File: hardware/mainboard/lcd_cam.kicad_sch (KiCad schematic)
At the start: 59 parts, among them U17 PCA9306, U18 PCA9306, U19 ADP5070ACPZ, U20 CAT4106HV4

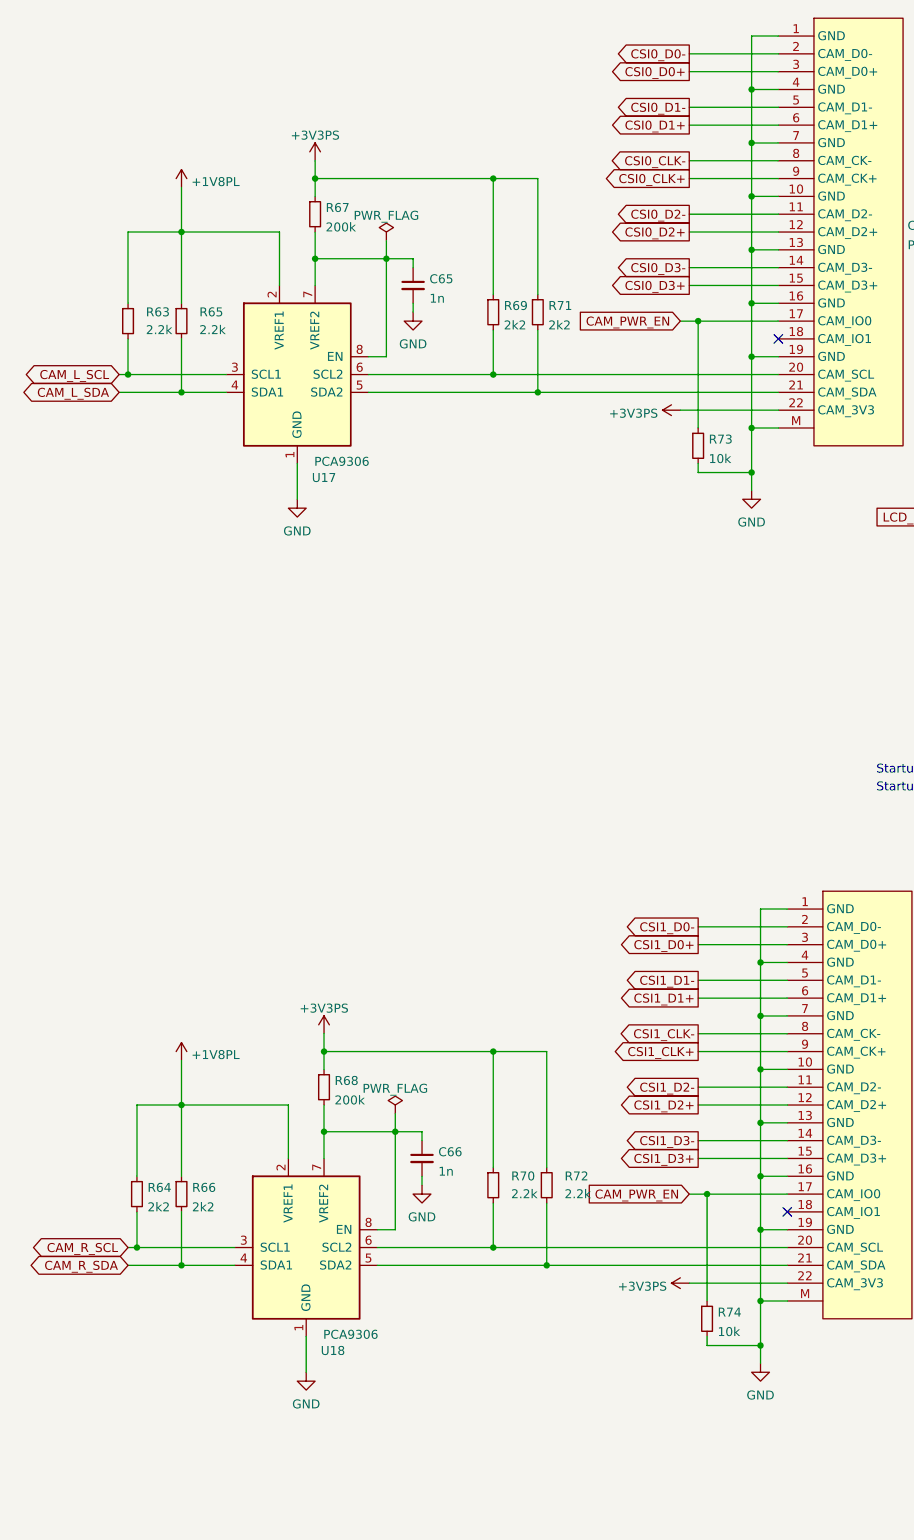
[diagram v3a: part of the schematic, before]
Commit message: Rework power arch to add 3V3PL; 5x PL RGB LEDs
Signed-off-by: gatecat <gatecat@ds0.me>
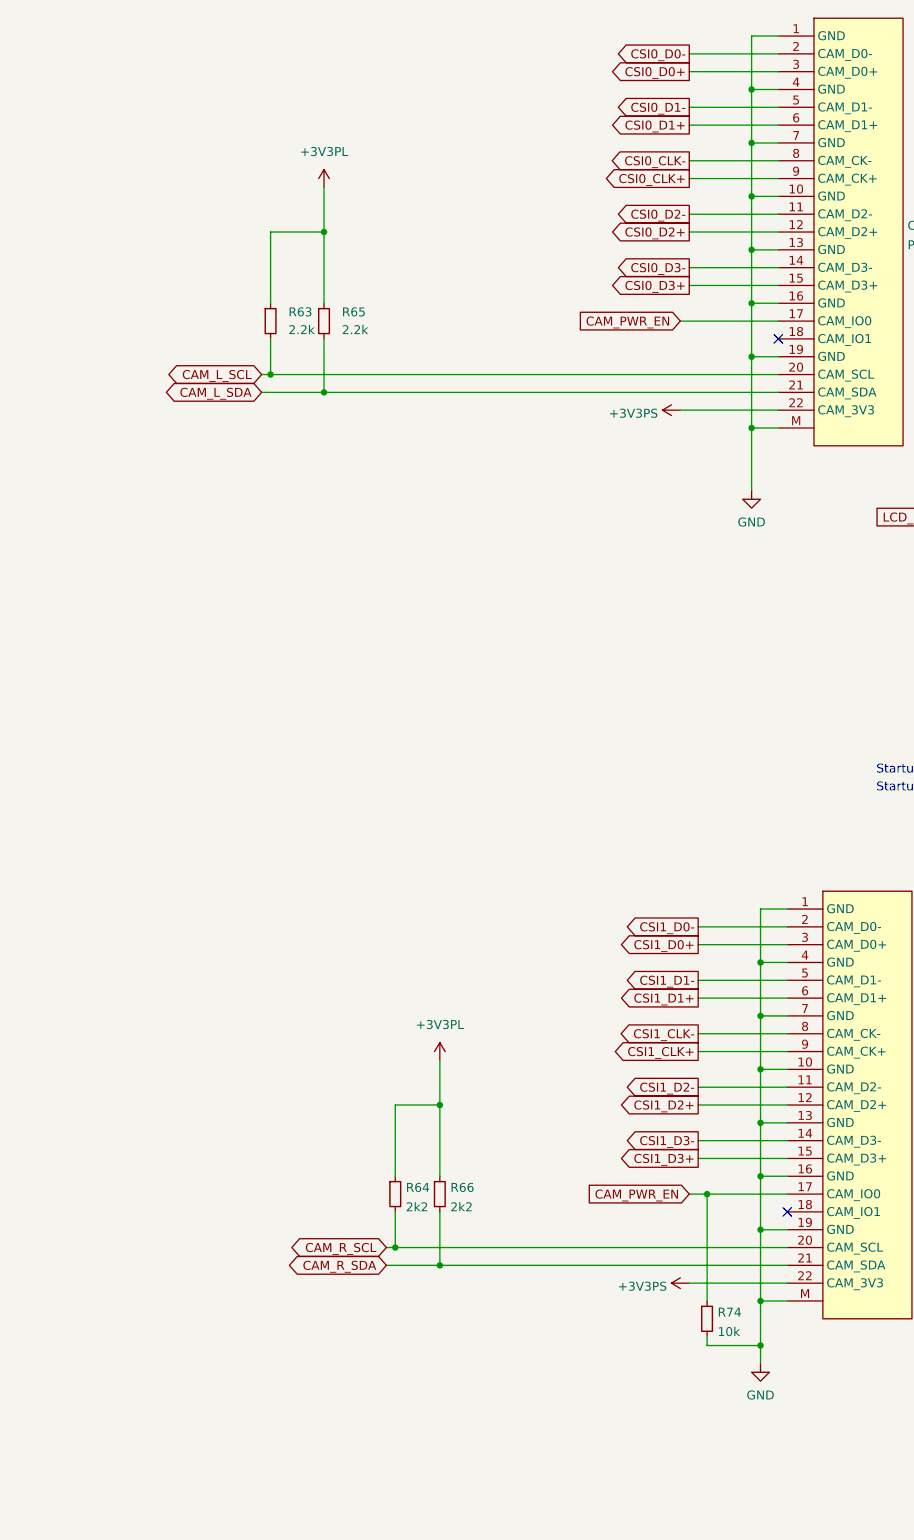
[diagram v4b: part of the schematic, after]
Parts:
- removed C65, C66: 1n, Capacitor_SMD:C_0402_1005Metric, symbol Device:C_Small
- removed R67, R68: 200k, Resistor_SMD:R_0402_1005Metric, symbol Device:R_Small
- removed R69, R71: 2k2, Resistor_SMD:R_0402_1005Metric, symbol Device:R_Small
- removed R70, R72: 2.2k, Resistor_SMD:R_0402_1005Metric, symbol Device:R_Small
- removed R73: 10k, Resistor_SMD:R_0402_1005Metric, symbol Device:R_Small
- removed U17, U18: PCA9306, Package_SO:TSSOP-8_3x3mm_P0.65mm, symbol Interface:PCA9306
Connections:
- net +1V8PL: no longer R63.1, R64.1, R65.1, R66.1
- net +3V3PS: now also R63.1, R64.1, R65.1, R66.1
- net CAM_L_SCL: now also CAM1.20 (CAM_SCL)
- net CAM_L_SDA: now also CAM1.21 (CAM_SDA)
- net CAM_R_SCL: now also CAM2.20 (CAM_SCL)
- net CAM_R_SDA: now also CAM2.21 (CAM_SDA)
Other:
- moved on the sheet: R63, R64, R65, R66

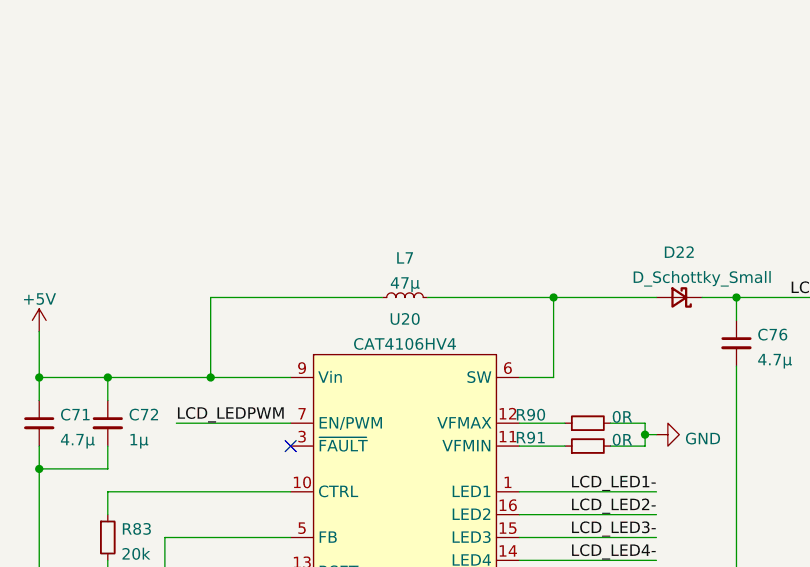
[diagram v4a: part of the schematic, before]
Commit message: Footprint assignment updates
Signed-off-by: gatecat <gatecat@ds0.me>
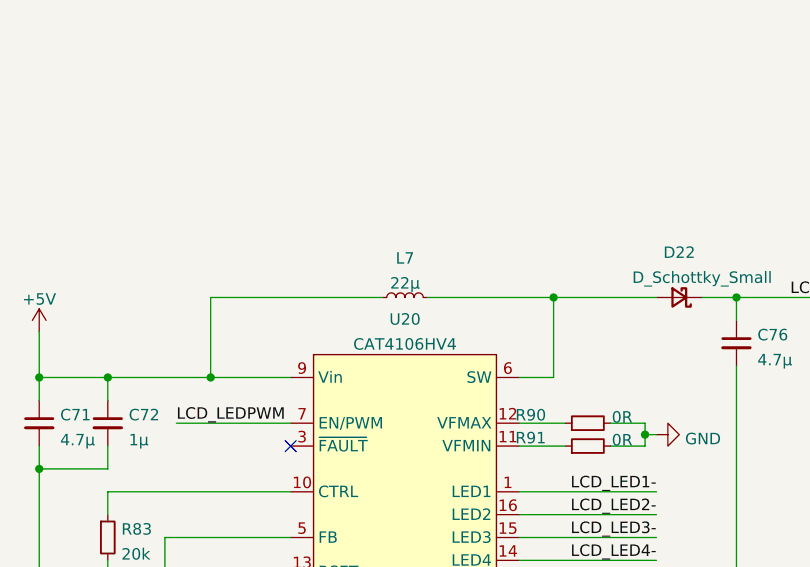
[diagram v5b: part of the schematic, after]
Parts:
- L7: value 47µ -> 22µ; footprint (none) -> Inductor_SMD:L_Taiyo-Yuden_NR-50xx
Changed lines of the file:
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@@
     (in_bom yes) (on_board yes)
     (property "Reference" "L7" (id 0) (at 234.95 197.5824 90))
-    (property "Value" "47µ" (id 1) (at 234.95 200.3575 90))
-    (property "Footprint" "" (id 2) (at 234.95 201.93 0)
+    (property "Value" "22µ" (id 1) (at 234.95 200.3575 90))
+    (property "Footprint" "Inductor_SMD:L_Taiyo-Yuden_NR-50xx" (id 2) (at 234.95 201.93 0)
       (effects (font (size 1.27 1.27)) hide)
     )

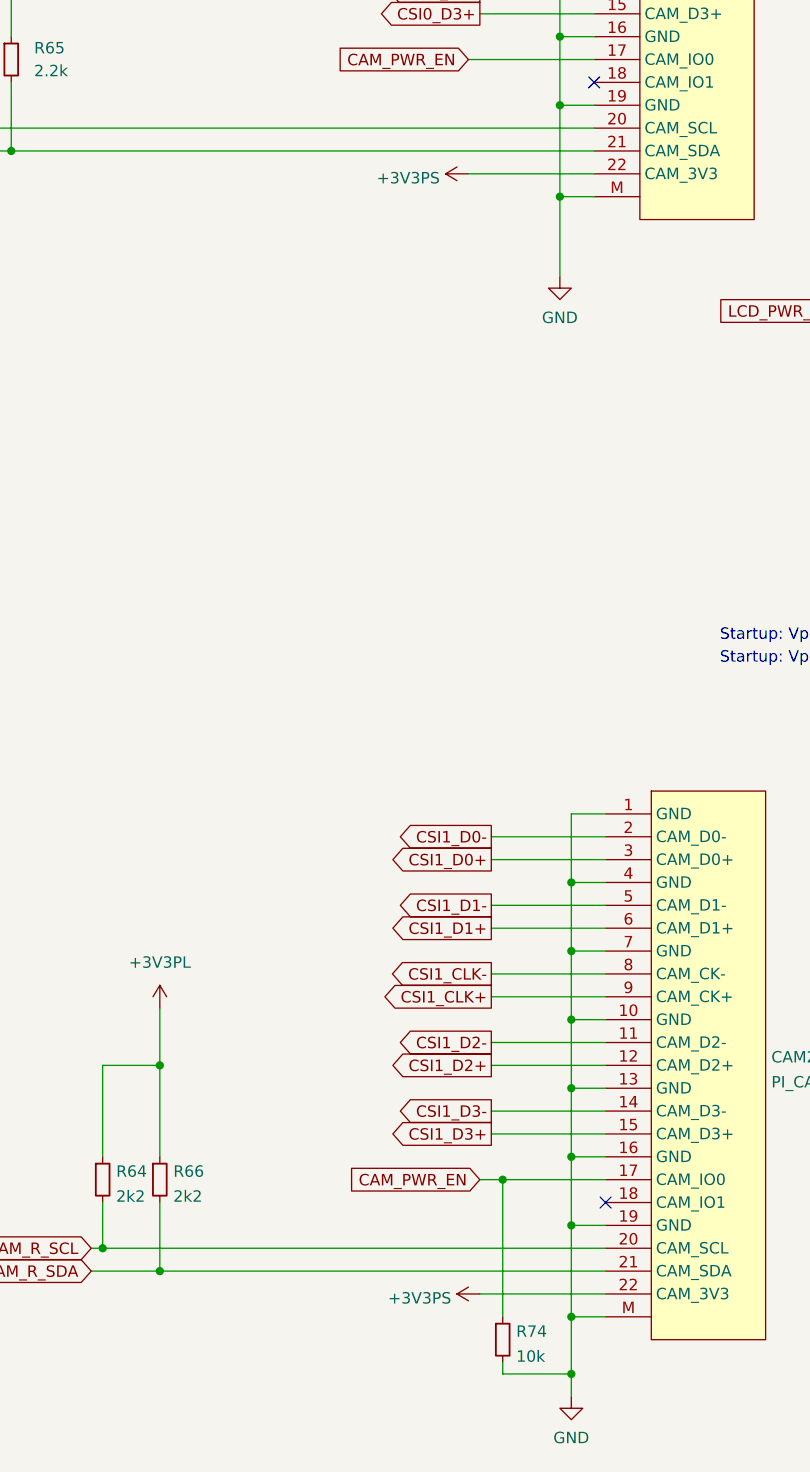
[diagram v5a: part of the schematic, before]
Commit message: Add separate reg for 3V3PL
Signed-off-by: gatecat <gatecat@ds0.me>
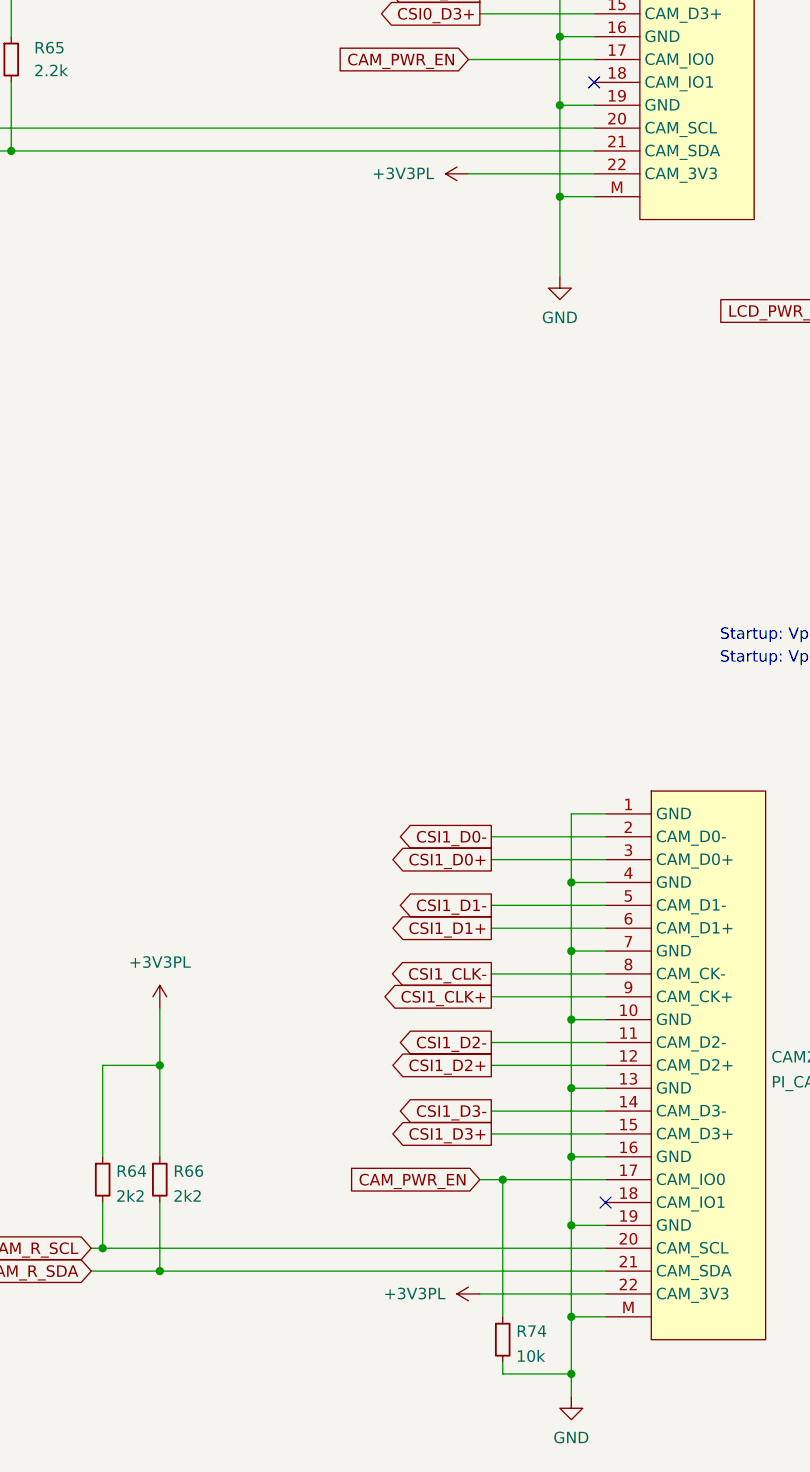
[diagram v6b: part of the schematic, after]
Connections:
- net +3V3PS renamed +3V3PL
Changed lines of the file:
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@@
     (pin "M")
-  )
-  (symbol (lib_id "meowality:+3V3PS") (at 123.19 82.55 90) (unit 1)
-    (in_bom yes) (on_board yes) (fields_autoplaced)
-    (property "Reference" "#PWR0351" (id 0) (at 127 82.55 0)
-      (effects (font (size 1.27 1.27)) hide)
-    )
-    (property "Value" "+3V3PS" (id 1) (at 120.015 83.029 90)
-      (effects (font (size 1.27 1.27)) (justify left))
-    )
-    (property "Footprint" "" (id 2) (at 123.19 82.55 0)
-      (effects (font (size 1.27 1.27)) hide)
-    )
-    (property "Datasheet" "" (id 3) (at 123.19 82.55 0)
-      (effects (font (size 1.27 1.27)) hide)
-    )
-    (pin "1")
   )
   (symbol (lib_id "Device:D_Schottky_Small") (at 248.92 102.87 180) (unit 1)
@@
     (pin "1")
     (pin "2")
+  )
+  (symbol (lib_id "meowality:+3V3PL") (at 124.46 207.01 90) (unit 1)
+    (in_bom yes) (on_board yes) (fields_autoplaced)
+    (property "Reference" "#PWR0299" (id 0) (at 128.27 207.01 0)
+      (effects (font (size 1.27 1.27)) hide)
+    )
+    (property "Value" "+3V3PL" (id 1) (at 120.65 207.0099 90)
+      (effects (font (size 1.27 1.27)) (justify left))
+    )
+    (property "Footprint" "" (id 2) (at 124.46 207.01 0)
+      (effects (font (size 1.27 1.27)) hide)
+    )
+    (property "Datasheet" "" (id 3) (at 124.46 207.01 0)
+      (effects (font (size 1.27 1.27)) hide)
+    )
+    (pin "1")
   )
   (symbol (lib_id "meowality:+3V3PL") (at 88.9 175.26 0) (unit 1)
@@
     (pin "1")
   )
+  (symbol (lib_id "meowality:+3V3PL") (at 123.19 82.55 90) (unit 1)
+    (in_bom yes) (on_board yes) (fields_autoplaced)
+    (property "Reference" "#PWR0108" (id 0) (at 127 82.55 0)
+      (effects (font (size 1.27 1.27)) hide)
+    )
+    (property "Value" "+3V3PL" (id 1) (at 119.38 82.5499 90)
+      (effects (font (size 1.27 1.27)) (justify left))
+    )
+    (property "Footprint" "" (id 2) (at 123.19 82.55 0)
+      (effects (font (size 1.27 1.27)) hide)
+    )
+    (property "Datasheet" "" (id 3) (at 123.19 82.55 0)
+      (effects (font (size 1.27 1.27)) hide)
+    )
+    (pin "1")
+  )
   (symbol (lib_id "Device:R_Small") (at 64.77 69.85 0) (unit 1)
     (in_bom yes) (on_board yes) (fields_autoplaced)
@@
     (pin "2")
   )
-  (symbol (lib_id "meowality:+3V3PS") (at 124.46 207.01 90) (unit 1)
-    (in_bom yes) (on_board yes) (fields_autoplaced)
-    (property "Reference" "#PWR0353" (id 0) (at 128.27 207.01 0)
-      (effects (font (size 1.27 1.27)) hide)
-    )
-    (property "Value" "+3V3PS" (id 1) (at 121.285 207.489 90)
-      (effects (font (size 1.27 1.27)) (justify left))
-    )
-    (property "Footprint" "" (id 2) (at 124.46 207.01 0)
-      (effects (font (size 1.27 1.27)) hide)
-    )
-    (property "Datasheet" "" (id 3) (at 124.46 207.01 0)
-      (effects (font (size 1.27 1.27)) hide)
-    )
-    (pin "1")
-  )
   (symbol (lib_id "meowality:CAT4106HV4") (at 234.95 241.3 0) (unit 1)
